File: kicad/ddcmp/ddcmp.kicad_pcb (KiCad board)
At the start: 2 copper layers, 114.6 x 73.7 mm, 35 parts, among them J1 UART, J2 RX, J3 TX, J4 TEST, J5 DTE, J6 DCE, J7 Bulkhead, U1 Pico, U2 max3491ecpd, U3 MAX3222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

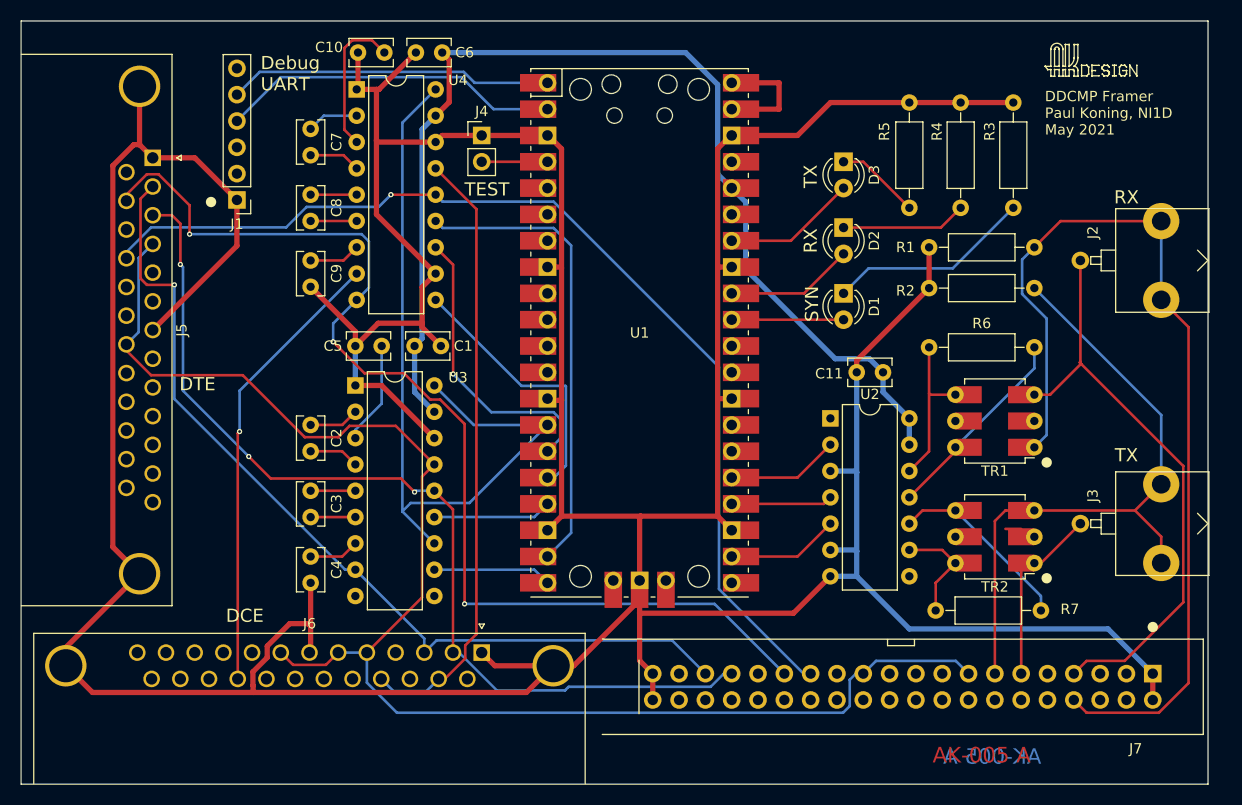
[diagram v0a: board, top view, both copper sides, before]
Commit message: Documentation improvements, small schematic fixes. Also firmware improvements, particularly clock rate accuracy.
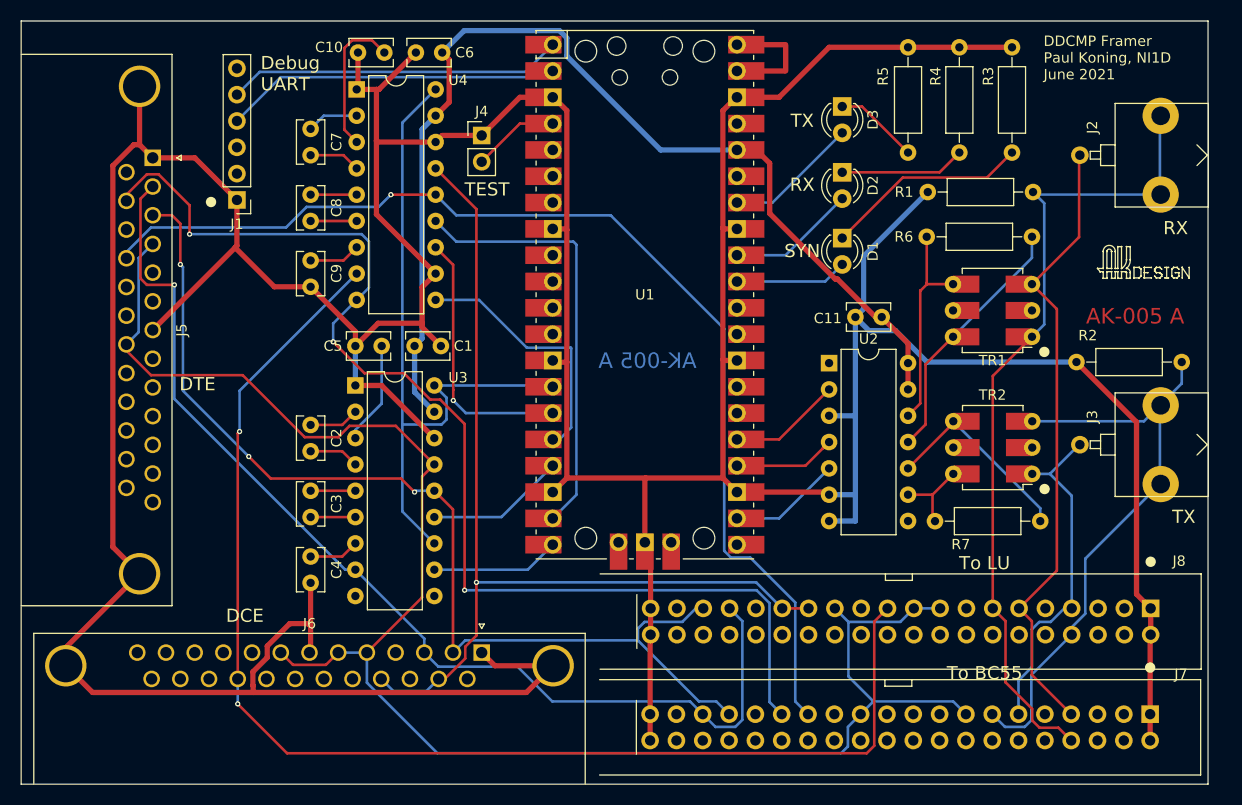
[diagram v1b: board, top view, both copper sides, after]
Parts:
- added J8: To LU, ddcmp_parts:Berg_40_pin_DEC_pinout, F.Cu at (142.0, 156.8)
- J7: value Bulkhead -> To BC55
- moved REF** 20.2 mm to (136.9, 124.9)
- moved R2 15.9 mm to (145.0, 133.0)
- moved R6 10.7 mm to (120.4, 120.9)
- moved TR1 10.7 mm to (126.8, 128.0)
- moved J2 10.2 mm to (135.2, 113.0)
- moved R7 8.62 mm to (121.2, 148.3)
- moved TR2 8.61 mm to (126.8, 141.2)
- moved J3 7.62 mm to (135.2, 141.0)
- moved C11 5.34 mm to (116.1, 128.7)
- moved D2 5.34 mm to (112.3, 114.7)
- moved D3 5.34 mm to (112.3, 108.3)
- moved R1 5.34 mm to (130.7, 116.6)
- moved R3 5.34 mm to (128.7, 112.8)
- moved R4 5.34 mm to (123.6, 112.8)
- moved R5 5.34 mm to (118.6, 112.8)
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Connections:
- net /Integral modem/IM_RDX renamed /Integral modem/IM_RXD
- net /Integral modem/IM_TDX renamed /Integral modem/IM_TXD
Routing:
- net /RS-232 I/O/RS232_0: track 43.9 -> 123.8 mm, vias 1 -> 2
- net /RS-232 I/O/CLKOUT: track 59.3 -> 92.4 mm, vias 0 -> 1
- net GND: track 504.9 -> 528.9 mm
- net /RS-232 I/O/RS232_1: track 142.9 -> 163.8 mm
- net /Integral modem/IM_TXD: track 18.0 -> 34.8 mm
- net /RS-232 I/O/TXD: track 88.0 -> 104.3 mm
- net /Integral modem/IM_RXD_N: track 93.0 -> 79.6 mm
- net /CPU/RS232_ENABLE: track 76.4 -> 66.1 mm
- net /RS-232 I/O/RXD: track 93.3 -> 102.5 mm
- net /RS-232 I/O/RXCLK: track 101.0 -> 108.6 mm
- net /RS-232 I/O/TXCLK: track 107.5 -> 113.7 mm
- net V3_3: track 109.3 -> 103.8 mm
- net Net-(R6-Pad1): track 17.1 -> 22.3 mm
- net Net-(R6-Pad2): track 20.5 -> 25.7 mm
- net /Integral modem/IM_TXD_N: track 62.4 -> 58.1 mm
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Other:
- board text added: "DDCMP Framer Paul Koning, NI1D June 2021"
- board text added: "To BC55"
- board text added: "To LU"
- board text removed: "DDCMP Framer Paul Koning, NI1D May 2021"

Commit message: Small PCB tweaks.  This version appears to be ready for fab.
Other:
- board text added: "DDCMP Framer Paul Koning, NI1D July 2021"
- board text removed: "DDCMP Framer Paul Koning, NI1D June 2021"
